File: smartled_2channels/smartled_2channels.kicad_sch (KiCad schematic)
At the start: 95 parts, among them J2 Conn_01x02, Q1 Q_NMOS_GSD, SW1 SW_Push, U1 OC5028B, U2 MAX485E, U3 PY32F003F1xUx, U4 OC5864, U5 SGM2033-3.3, U6 OC5028B, U7 GS8521

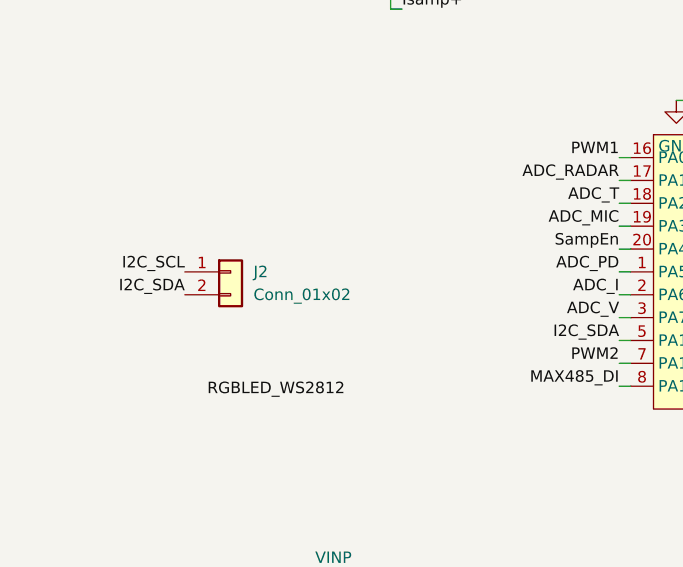
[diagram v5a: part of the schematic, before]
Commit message: 修改TP焊盘为0.6mm，引出I2C接口
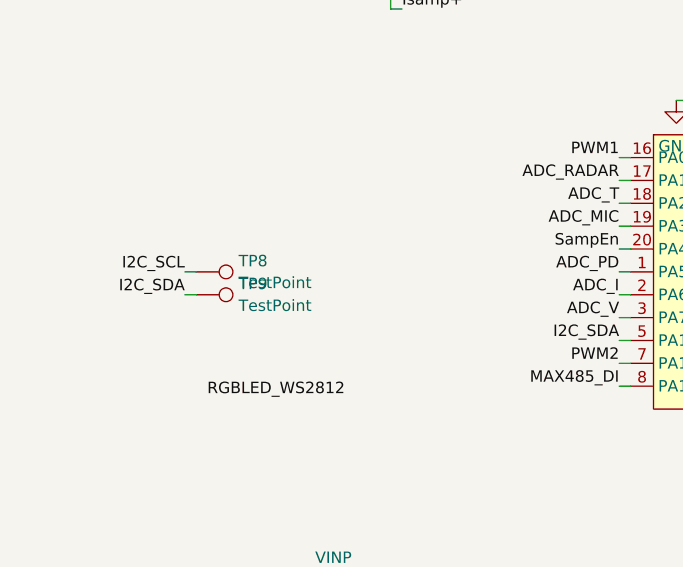
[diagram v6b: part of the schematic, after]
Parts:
- removed J2: Conn_01x02, Resistor_SMD:R_0603_1608Metric, symbol Connector_Generic:Conn_01x02
- added TP8, TP9: TestPoint, project_footprints:1Pad_0.6mm, symbol Connector:TestPoint
- C16: footprint Capacitor_SMD:C_0402_1005Metric -> Capacitor_SMD:C_0603_1608Metric
- TP1, TP2, TP3: footprint TestPoint:TestPoint_Pad_D1.0mm -> project_footprints:1Pad_0.6mm
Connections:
- net I2C_SCL: now also TP8.1
- net I2C_SDA: now also TP9.1
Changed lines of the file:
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@@
 	(wire
 		(pts
+			(xy 33.02 88.9) (xy 34.29 88.9)
+		)
+		(stroke
+			(width 0)
+			(type default)
+		)
+	)
+	(wire
+		(pts
 			(xy 66.04 48.26) (xy 66.04 49.53)
 		)
@@
 	(wire
 		(pts
+			(xy 33.02 91.44) (xy 34.29 91.44)
+		)
+		(stroke
+			(width 0)
+			(type default)
+		)
+	)
+	(wire
+		(pts
 			(xy 205.74 146.05) (xy 205.74 144.78)
 		)
@@
 			)
 		)
-		(property "Footprint" "TestPoint:TestPoint_Pad_D1.0mm"
+		(property "Footprint" "project_footprints:1Pad_0.6mm"
 			(at 256.54 157.48 0)
 			(effects
@@
 	)
 	(symbol
-		(lib_id "Connector_Generic:Conn_01x02")
-		(at 38.1 88.9 0)
-		(unit 1)
-		(exclude_from_sim no)
-		(in_bom yes)
-		(on_board yes)
-		(dnp no)
-		(fields_autoplaced yes)
-		(property "Reference" "J2"
-			(at 40.64 88.8999 0)
-			(effects
-				(font
-					(size 1.27 1.27)
-				)
-				(justify left)
-			)
-		)
-		(property "Value" "Conn_01x02"
-			(at 40.64 91.4399 0)
-			(effects
-				(font
-					(size 1.27 1.27)
-				)
-				(justify left)
-			)
-		)
-		(property "Footprint" "Resistor_SMD:R_0603_1608Metric"
-			(at 38.1 88.9 0)
-			(effects
-				(font
-					(size 1.27 1.27)
-				)
-				(hide yes)
-			)
-		)
-		(property "Datasheet" "~"
-			(at 38.1 88.9 0)
-			(effects
-				(font
-					(size 1.27 1.27)
-				)
-				(hide yes)
-			)
-		)
-		(property "Description" "Generic connector, single row, 01x02, script generated (kicad-library-utils/schlib/autogen/connector/)"
-			(at 38.1 88.9 0)
-			(effects
-				(font
-					(size 1.27 1.27)
-				)
-				(hide yes)
-			)
-		)
-		(pin "1"
-		)
-		(pin "2"
-		)
-		(instances
-			(project "smartled_2channels"
-				(path "/03135fe0-800a-4910-99f5-abc1a6d2d96f"
-					(reference "J2")
-					(unit 1)
-				)
-			)
-		)
-	)
-	(symbol
 		(lib_id "Device:C_Small")
 		(at 34.29 130.81 90)
@@
 			)
 		)
-		(property "Footprint" "TestPoint:TestPoint_Pad_D1.0mm"
+		(property "Footprint" "project_footprints:1Pad_0.6mm"
 			(at 256.54 162.56 0)
 			(effects
@@
 	)
 	(symbol
+		(lib_id "Connector:TestPoint")
+		(at 34.29 91.44 270)
+		(unit 1)
+		(exclude_from_sim no)
+		(in_bom yes)
+		(on_board yes)
+		(dnp no)
+		(fields_autoplaced yes)
+		(property "Reference" "TP9"
+			(at 38.989 90.2278 90)
+			(effects
+				(font
+					(size 1.27 1.27)
+				)
+				(justify left)
+			)
+		)
+		(property "Value" "TestPoint"
+			(at 38.989 92.6521 90)
+			(effects
+				(font
+					(size 1.27 1.27)
+				)
+				(justify left)
+			)
+		)
+		(property "Footprint" "project_footprints:1Pad_0.6mm"
+			(at 34.29 96.52 0)
+			(effects
+				(font
+					(size 1.27 1.27)
+				)
+				(hide yes)
+			)
+		)
+		(property "Datasheet" "~"
+			(at 34.29 96.52 0)
+			(effects
+				(font
+					(size 1.27 1.27)
+				)
+				(hide yes)
+			)
+		)
+		(property "Description" "test point"
+			(at 34.29 91.44 0)
+			(effects
+				(font
+					(size 1.27 1.27)
+				)
+				(hide yes)
+			)
+		)
+		(pin "1"
+		)
+		(instances
+			(project "smartled_2channels"
+				(path "/03135fe0-800a-4910-99f5-abc1a6d2d96f"
+					(reference "TP9")
+					(unit 1)
+				)
+			)
+		)
+	)
+	(symbol
 		(lib_id "power:+5V")
 		(at 80.01 129.54 0)
@@
 			)
 		)
-		(property "Footprint" "Capacitor_SMD:C_0402_1005Metric"
+		(property "Footprint" "Capacitor_SMD:C_0603_1608Metric"
 			(at 91.44 69.85 0)
 			(effects
@@
 	)
 	(symbol
+		(lib_id "Connector:TestPoint")
+		(at 34.29 88.9 270)
+		(unit 1)
+		(exclude_from_sim no)
+		(in_bom yes)
+		(on_board yes)
+		(dnp no)
+		(fields_autoplaced yes)
+		(property "Reference" "TP8"
+			(at 38.989 87.6878 90)
+			(effects
+				(font
+					(size 1.27 1.27)
+				)
+				(justify left)
+			)
+		)
+		(property "Value" "TestPoint"
+			(at 38.989 90.1121 90)
+			(effects
+				(font
+					(size 1.27 1.27)
+				)
+				(justify left)
+			)
+		)
+		(property "Footprint" "project_footprints:1Pad_0.6mm"
+			(at 34.29 93.98 0)
+			(effects
+				(font
+					(size 1.27 1.27)
+				)
+				(hide yes)
+			)
+		)
+		(property "Datasheet" "~"
+			(at 34.29 93.98 0)
+			(effects
+				(font
+					(size 1.27 1.27)
+				)
+				(hide yes)
+			)
+		)
+		(property "Description" "test point"
+			(at 34.29 88.9 0)
+			(effects
+				(font
+					(size 1.27 1.27)
+				)
+				(hide yes)
+			)
+		)
+		(pin "1"
+		)
+		(instances
+			(project ""
+				(path "/03135fe0-800a-4910-99f5-abc1a6d2d96f"
+					(reference "TP8")
+					(unit 1)
+				)
+			)
+		)
+	)
+	(symbol
 		(lib_id "Device:R")
 		(at 212.09 93.98 0)
@@
 			)
 		)
-		(property "Footprint" "TestPoint:TestPoint_Pad_D1.0mm"
+		(property "Footprint" "project_footprints:1Pad_0.6mm"
 			(at 256.54 160.02 0)
 			(effects

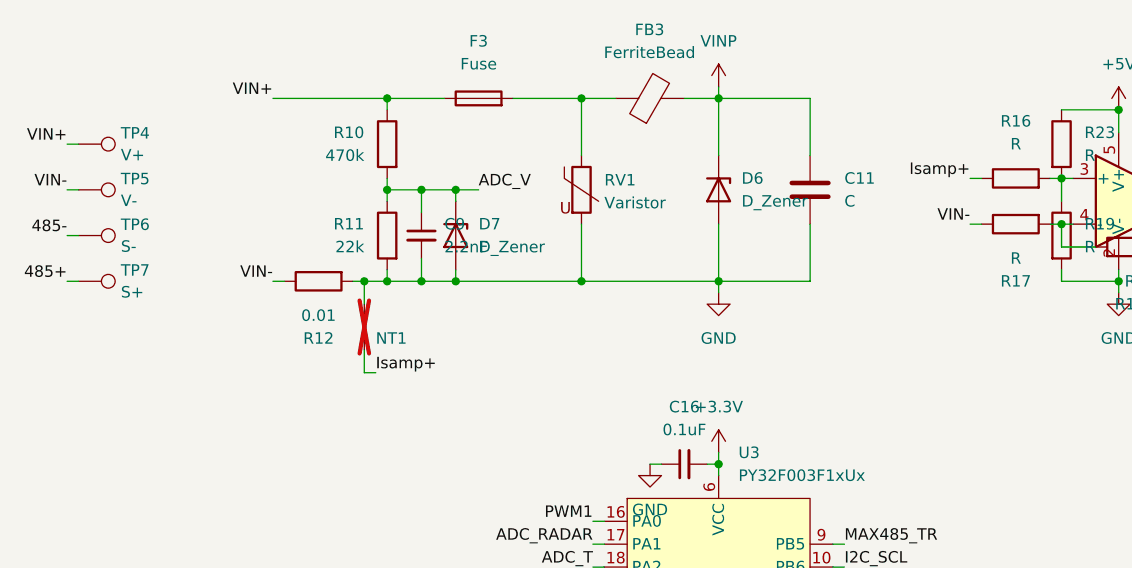
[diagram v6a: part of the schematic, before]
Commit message: 保险丝移动到负极
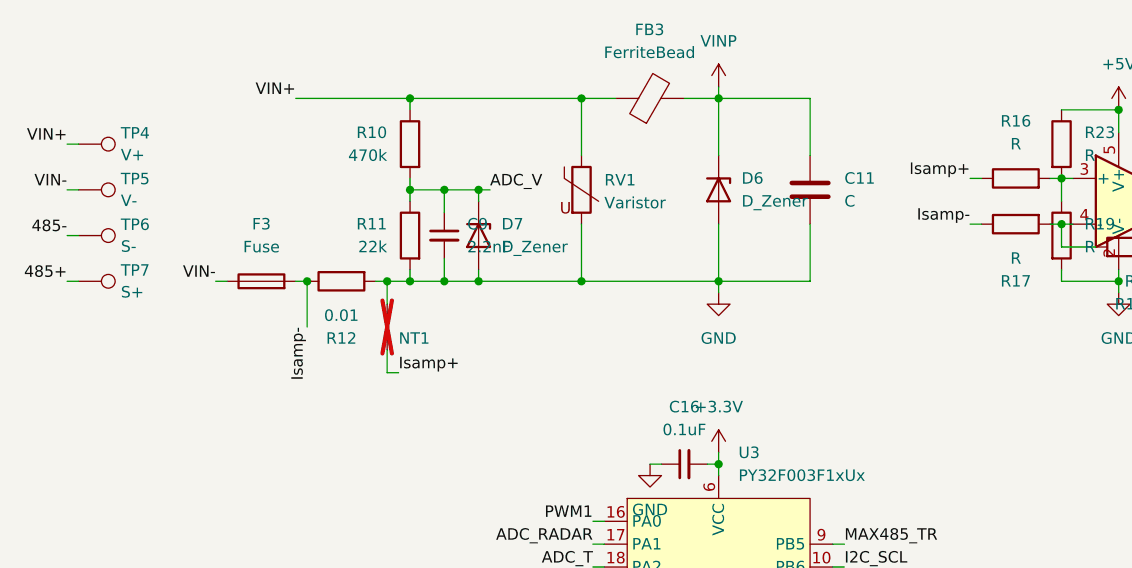
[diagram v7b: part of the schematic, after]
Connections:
- net VIN+: now also FB3.1, RV1.1; no longer F3.1
- net VIN-: now also F3.1; no longer R12.1, R17.1
- new net Isamp-: F3.2, R12.1, R17.1
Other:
- moved on the sheet: C9, D7, NT1, R10, R11, R12

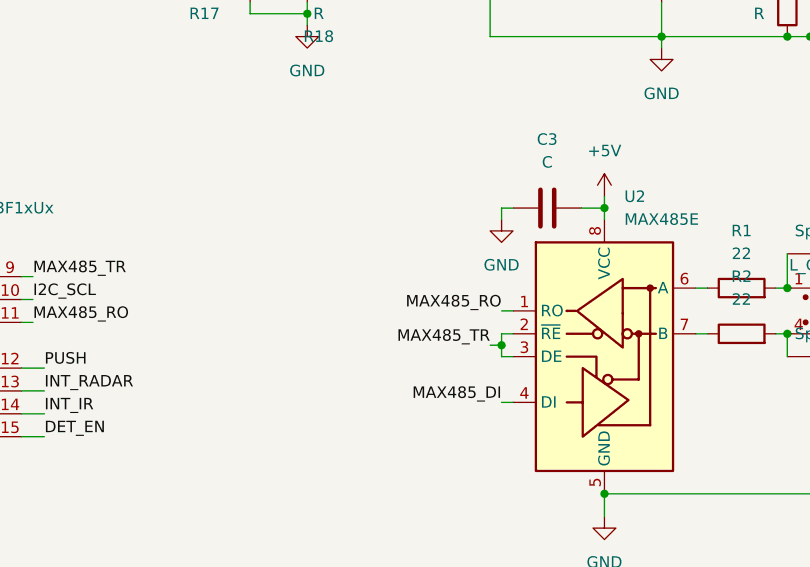
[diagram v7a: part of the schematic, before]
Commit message: MAX485 RO添加稳压二极管做电平转换
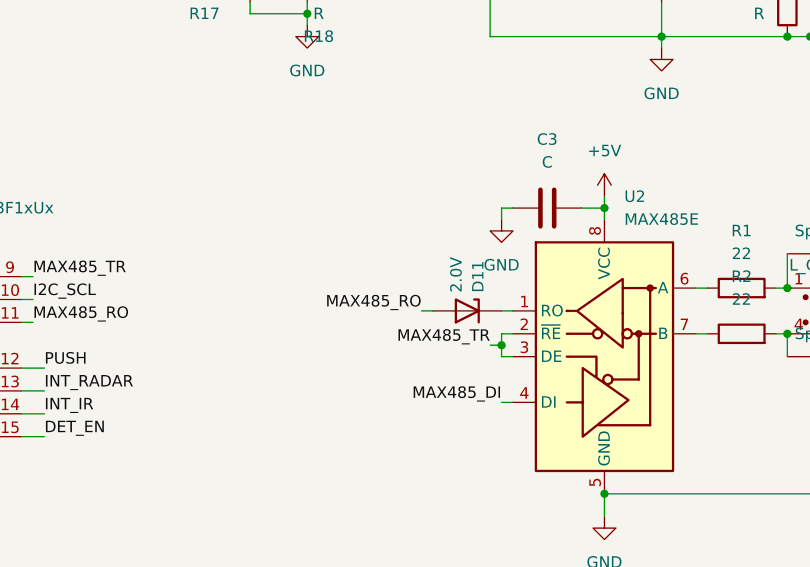
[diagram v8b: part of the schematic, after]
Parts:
- added D11: 2.0V, Diode_SMD:D_SOD-523, symbol Device:D_Zener
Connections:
- net MAX485_RO: now also D11.2 (A); no longer U2.1 (RO)
- new net: D11.1 (K), U2.1 (RO)
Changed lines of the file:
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@@
 	(wire
 		(pts
+			(xy 161.29 82.55) (xy 162.56 82.55)
+		)
+		(stroke
+			(width 0)
+			(type default)
+		)
+	)
+	(wire
+		(pts
 			(xy 227.33 133.35) (xy 228.6 133.35)
 		)
@@
 	(wire
 		(pts
-			(xy 161.29 82.55) (xy 162.56 82.55)
+			(xy 152.4 82.55) (xy 153.67 82.55)
 		)
 		(stroke
@@
 	)
 	(label "MAX485_RO"
-		(at 161.29 82.55 180)
+		(at 152.4 82.55 180)
 		(effects
 			(font
@@
 					(unit 1)
 				)
+			)
+		)
+	)
+	(symbol
+		(lib_id "Device:D_Zener")
+		(at 157.48 82.55 0)
+		(mirror y)
+		(unit 1)
+		(exclude_from_sim no)
+		(in_bom yes)
+		(on_board yes)
+		(dnp no)
+		(property "Reference" "D11"
+			(at 158.6922 80.518 90)
+			(effects
+				(font
+					(size 1.27 1.27)
+				)
+				(justify left)
+			)
+		)
+		(property "Value" "2.0V"
+			(at 156.2679 80.518 90)
+			(effects
+				(font
+					(size 1.27 1.27)
+				)
+				(justify left)
+			)
+		)
+		(property "Footprint" "Diode_SMD:D_SOD-523"
+			(at 157.48 82.55 0)
+			(effects
+				(font
+					(size 1.27 1.27)
+				)
+				(hide yes)
+			)
+		)
+		(property "Datasheet" "~"
+			(at 157.48 82.55 0)
+			(effects
+				(font
+					(size 1.27 1.27)
+				)
+				(hide yes)
+			)
+		)
+		(property "Description" "Zener diode"
+			(at 157.48 82.55 0)
+			(effects
+				(font
+					(size 1.27 1.27)
+				)
+				(hide yes)
+			)
+		)
+		(pin "1"
+		)
+		(pin "2"
+		)
+		(instances
+			(project "smartled_2channels"
+				(path "/03135fe0-800a-4910-99f5-abc1a6d2d96f"
+					(reference "D11")
+					(unit 1)
+				)
